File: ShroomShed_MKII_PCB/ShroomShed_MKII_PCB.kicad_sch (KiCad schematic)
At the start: 68 parts, among them J1 SWD 14 pin header, J2 TYPE-C-31-M-12, J3 Fan, J4 AUX_SPI, J5 SD_SPI, J6 DHT_I2C, J7 Display_Touch_SPI, J8 Front_Panel, J9 Transducer Driver, Q1 T2N7002AK, Q2 BC817, SW1 EVQ-Q2B03W, SW2 SW_SPDT, U1 AMS1117-3.3, U2 TPS61085DGK, U3 USBLC6-2SC6, U4 ENS210, U5 STM32H562VGTx, Y1 16MHz

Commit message: added solidworks files
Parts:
- removed J8: Front_Panel, DOWNLOAD_Connectors:CONN_532610001-SD_06_MOL, symbol Connector_Generic:Conn_01x06
- removed SW2: SW_SPDT, Button_Switch_SMD:SW_SPDT_PCM12, symbol Switch:SW_SPDT
- added J9: Control_Panel, DOWNLOAD_Connectors:CONN_532610001-SD_07_MOL, symbol Connector_Generic:Conn_01x07
- added SW3: FAN P SELECT, footprints:MST-22D18G2 3J, symbol Switch:SW_Push_SPDT
- C11: value 1000uf -> 1000uF
- C12, C14, C15: value 10uf -> 10uF
- C13: value 1uf -> 1uF
- C18, C20: value 100nf -> 100nF
- C19: value 1.1nf -> 1.1nF
- J4: JLCPCB Part # (none) -> C17393620
- J5, J6: JLCPCB Part # (none) -> C696092
- J7: JLCPCB Part # (none) -> C505101
- J8: renamed from J9; JLCPCB Part # (none) -> C293630
- R12: value 1K -> 1k
- renumbered D6 to D3, D3 to D4, R21 to R13, R13 to R14, R14 to R15, R15 to R16
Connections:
- net +3V3: now also SW3.1 (A)
- net ENCODER_BUTTON: now also J9.5 (Pin_5)
- net ENCODER_CHANNEL_A: now also J9.6 (Pin_6)
- net ENCODER_CHANNEL_B: now also J9.7 (Pin_7)
- net GND: now also J9.1 (Pin_1), SW3.3 (C)
- net LED_WATER: now also U5.83 (PD2), J9.2 (Pin_2); no longer U5.84 (PD3)
- net PUSH_BUTTON renamed BUTTON_1
- net BUTTON_1: now also J9.4 (Pin_4)
- new net BUTTON_2: J9.3 (Pin_3), U5.84 (PD3)

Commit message: source code template setup and blinky achieved
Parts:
- removed D3: Blue, LED_SMD:LED_0603_1608Metric, symbol Device:LED
- removed J4: AUX_SPI, DOWNLOAD_Connectors:CONN_532610001-SD_06_MOL, symbol Connector_Generic:Conn_01x06
- removed R13: 330r, Resistor_SMD:R_0603_1608Metric, symbol Device:R_Small
- removed R17: 2k2, Resistor_SMD:R_0603_1608Metric, symbol Device:R_Small
- added D5: TC5050RGBF08-3CJH-AF53A, symbol Custom_Symbols:LED_RGB_TC5050RGBF08
- added J4: SD_SPI, DOWNLOAD_Connectors:CONN_532610001-SD_04_MOL, symbol Connector_Generic:Conn_01x04
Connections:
- net +3V3: now also J4.1 (Pin_1)
- net GND: now also J4.4 (Pin_4); no longer Q2.2 (E)
- net SPI2_MISO: no longer names the net of U5.53 (PB14)
- net SPI2_MOSI: no longer names the net of U5.54 (PB15)
- net SPI2_NSS renamed UART5_RX
- net UART5_RX: now also J4.3 (Pin_3)
- net SPI2_SCK renamed UART5_TX
- net UART5_TX: now also J4.2 (Pin_2)
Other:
- note removed: "Humidifier LED"
- moved on the sheet: Q2

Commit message: finished V2.1 PCB
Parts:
- removed D4: Yellow, LED_SMD:LED_0603_1608Metric, symbol Device:LED
- removed J3: Fan, Connector_JST:JST_XH_B2B-XH-A_1x02_P2.50mm_Vertical, symbol Connector:Screw_Terminal_01x02
- removed J8: Transducer Driver, DOWNLOAD_Connectors:CONN_532610001-SD_03_MOL, symbol Connector_Generic:Conn_01x03
- removed J9: Control_Panel, DOWNLOAD_Connectors:CONN_532610001-SD_07_MOL, symbol Connector_Generic:Conn_01x07
- removed Q1: T2N7002AK, Package_TO_SOT_SMD:SOT-23, symbol Transistor_FET:T2N7002AK
- removed Q2: BC817, Package_TO_SOT_SMD:SOT-23, symbol Transistor_BJT:BC817
- removed R16: 10k, Resistor_SMD:R_0603_1608Metric, symbol Device:R
- removed R7: 2k2, Resistor_SMD:R_0603_1608Metric, symbol Device:R_Small
- added C2, C3, C7, C8: 1uF, Capacitor_SMD:C_0603_1608Metric, symbol Device:C
- added D10, D11, D12, D13, D2, D3, D4, D5, D6, D8, D9: XL-5050RGBC, LED_SMD:LED_RGB_5050-6, symbol Custom:XL-5050RGBC
- added D14: BLUE, LED_THT:LED_D4.0mm, symbol Device:LED
- added H1, H4: MountingHole_Pad, MountingHole:MountingHole_3.2mm_M3_Pad, symbol Mechanical:MountingHole_Pad
- added J3: Inputs, Connector_JST:JST_XH_B6B-XH-A_1x06_P2.50mm_Vertical, symbol Connector_Generic:Conn_01x06
- added J6: ERM, Connector_JST:JST_XH_S4B-XH-A-1_1x04_P2.50mm_Horizontal, symbol Connector_Generic:Conn_01x04
- added Q1: BC817, Package_TO_SOT_SMD:SOT-23, symbol Transistor_BJT:BC817
- added R1: 33r, Resistor_SMD:R_0603_1608Metric, symbol Device:R_Small
- added R11, R3, R4: 4k7, Resistor_SMD:R_0603_1608Metric, symbol Device:R_Small
- added R13: 5k1, Resistor_SMD:R_0603_1608Metric, symbol Device:R_Small
- added R16: 500r, Resistor_SMD:R_0603_1608Metric, symbol Device:R_Small
- added R17, R20: 10k, Resistor_SMD:R_0603_1608Metric, symbol Device:R_Small
- added U1, U2, U5, U6: WS2811, Package_SO:SOIC-8_3.9x4.9mm_P1.27mm, symbol Driver_LED:WS2811
- C15: renamed from C11; value 1000uF -> 470uF; footprint Capacitor_SMD:CP_Elec_10x10.5 -> Capacitor_SMD:CP_Elec_6.3x7.7; P# C5355001 -> C2977552
- D1: renamed from D5; value TC5050RGBF08-3CJH-AF53A -> XL-5050RGBC; footprint (none) -> LED_SMD:LED_RGB_5050-6; symbol Custom_Symbols:LED_RGB_TC5050RGBF08 -> Custom:XL-5050RGBC
- J2: renamed from J4; value SD_SPI -> UART; footprint DOWNLOAD_Connectors:CONN_532610001-SD_04_MOL -> Connector_PinHeader_2.00mm:PinHeader_1x04_P2.00mm_Vertical
- J4: renamed from J6; value DHT_I2C -> SHT31; footprint DOWNLOAD_Connectors:CONN_532610001-SD_04_MOL -> Connector_JST:JST_XH_S4B-XH-A-1_1x04_P2.50mm_Horizontal
- J7: renamed from J5; footprint DOWNLOAD_Connectors:CONN_532610001-SD_04_MOL -> Connector_PinSocket_2.54mm:PinSocket_1x04_P2.54mm_Vertical
- J8: renamed from J7; footprint DOWNLOAD_Connectors:CONN_532610001-SD_14_MOL -> Connector_PinSocket_2.54mm:PinSocket_1x14_P2.54mm_Vertical
- R10: value 2k2 -> 4k7
- R12: value 1k -> 5k1; DESCRIPTION C21190 -> (none); PACKAGE 0603 -> (none)
- R15: value 100R -> 1k; DESCRIPTION C22775 -> (none); PACKAGE 0603 -> (none)
- R18: renamed from R9; value 47r -> 33r
- SW2: renamed from SW3; value FAN P SELECT -> BOOT SELECT; footprint footprints:MST-22D18G2 3J -> Button_Switch_SMD:SW_SPDT_Shouhan_MSK12C02; P# (none) -> C431540
- renumbered C12 to C1, C15 to C10, C10 to C11, C20 to C12, C21 to C13, C22 to C14, C8 to C16, C9 to C17, C23 to C18, C24 to C19, C7 to C20, C1 to C21, C16 to C22, C2 to C23, C3 to C24, C17 to C25, C4 to C26, C5 to C27, C6 to C28, C13 to C4, C18 to C5, C19 to C6, C14 to C9, D1 to D15, D2 to D7, H1 to H3, J2 to J1, J1 to J5, R3 to R14, R14 to R19, R8 to R2, R4 to R21, R11 to R6, R1 to R7, R6 to R8, R2 to R9, U2 to U3, U3 to U4, U4 to U7, U1 to U8, U5 to U9
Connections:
- net +12V: now also D1.4 (BA), D1.5 (GA), D1.6 (RA), R10.1, D11.4 (BA), D11.5 (GA), D11.6 (RA), D14.2 (A), D4.4 (BA), D4.5 (GA), D4.6 (RA), D8.4 (BA), D8.5 (GA), D8.6 (RA), J6.1 (Pin_1), R11.1, R3.1, R4.1; no longer R12.1
- net +3V3: now also J8.14 (Pin_14), R12.2, R13.2, R17.1, R20.1; no longer J8.1 (Pin_1), R10.2
- net DISPLAY_DC: now also J8.10 (Pin_10); no longer J8.3 (Pin_3)
- net DISPLAY_LED: now also J8.7 (Pin_7), U9.95 (PB8); no longer J8.8 (Pin_8), U9.26 (PA3)
- net DISPLAY_MISO: now also J8.6 (Pin_6); no longer J8.5 (Pin_5)
- net DISPLAY_MOSI: now also J8.9 (Pin_9); no longer J8.6 (Pin_6)
- net DISPLAY_NSS: now also J8.12 (Pin_12); no longer J8.4 (Pin_4)
- net DISPLAY_RST: now also J8.11 (Pin_11); no longer J8.7 (Pin_7)
- net DISPLAY_SCK: now also J8.8 (Pin_8); no longer J8.2 (Pin_2)
- net ENCODER_CHANNEL_A: now also U9.60 (PD13), J3.1 (Pin_1); no longer U9.64 (PC7)
- net ENCODER_CHANNEL_B: now also U9.59 (PD12), J3.2 (Pin_2); no longer U9.63 (PC6)
- net ENS210_SCL: now also U9.47 (PB10), R13.1; no longer U9.92 (PB6)
- net ENS210_SDA: now also R12.1, U9.51 (PB12); no longer R10.1, U9.93 (PB7)
- net FAN_PWM: now also U9.36 (PB1), J6.3 (Pin_3); no longer R15.2, U9.24 (PA1)
- net GND: now also J8.13 (Pin_13), C2.2, C3.2, C7.2, C8.2, H1.1, H4.1, J3.6 (Pin_6), J6.4 (Pin_4), Q1.2 (E), U1.4 (GND), U2.4 (GND), U5.4 (GND), U6.4 (GND); no longer J8.14 (Pin_14)
- net SD_MISO: now also J7.2 (Pin_2), U9.31 (PA6); no longer J7.3 (Pin_3), U9.79 (PC11)
- net SD_MOSI: now also J7.3 (Pin_3), U9.32 (PA7); no longer J7.4 (Pin_4), U9.80 (PC12)
- net SD_NSS: now also J7.4 (Pin_4), U9.29 (PA4); no longer J7.1 (Pin_1), U9.77 (PA15(JTDI))
- net SD_SCK: now also J7.1 (Pin_1), U9.30 (PA5); no longer J7.2 (Pin_2), U9.78 (PC10)
- net SHT31_SCL: now also R20.2
- net SHT31_SDA: now also R17.2
- net SWD_SWO: no longer U9.89 (PB3(JTDO)
- net TOUCH_IRQ: now also J8.1 (Pin_1), U9.92 (PB6); no longer J8.13 (Pin_13), U9.33 (PC4)
- net TOUCH_MISO: now also J8.2 (Pin_2), U9.90 (PB4(NJTRST)); no longer J8.11 (Pin_11), U9.31 (PA6)
- net TOUCH_MOSI: now also J8.3 (Pin_3), U9.91 (PB5); no longer J8.12 (Pin_12), U9.32 (PA7)
- net TOUCH_NSS: now also J8.4 (Pin_4), U9.77 (PA15(JTDI)); no longer J8.9 (Pin_9), U9.29 (PA4)
- net TOUCH_SCK: now also J8.5 (Pin_5), U9.89 (PB3(JTDO); no longer J8.10 (Pin_10), U9.30 (PA5)
- net TRANSDUCER_PWM: now also U9.35 (PB0), J6.2 (Pin_2); no longer U9.44 (PE13)
- net UART4_RX: now also U9.81 (PD0); no longer U9.58 (PD11)
- net UART4_TX: now also U9.82 (PD1); no longer U9.59 (PD12)
- net WATER_LED: now reaches U9.16 (PC1)
- net WATER_LED: now also R15.2
- net RGB_MOSI: now reaches U9.18 (PC3)
- net RGB_MOSI: now also R1.1
- net RF_RX: now reaches U9.38 (PE7)
- net RF_RX: now also J2.3 (Pin_3)
- net RF_TX: now reaches U9.39 (PE8)
- net RF_TX: now also J2.2 (Pin_2)
- net INPUT_3: now reaches U9.56 (PD9)
- net INPUT_3: now also J3.5 (Pin_5)
- net INPUT_2: now reaches U9.57 (PD10)
- net INPUT_2: now also J3.4 (Pin_4)
- net at R15.1: now also Q1.1 (B)
- net at SW2.2 (B): now also R19.2
- net at D1.1 (RK): now also D2.6 (RA)
- net at D1.2 (GK): now also D2.5 (GA)
- net at D1.3 (BK): now also D2.4 (BA)
- net BUTTON_1: no longer names the net of U9.85 (PD4)
- net BUTTON_2: no longer names the net of U9.84 (PD3)
- net ENCODER_BUTTON: no longer names the net of U9.86 (PD5)
- net FAN_DETECT: no longer names the net of U9.25 (PA2)
- net LED_HUMIDIFIER: no longer names the net of U9.45 (PE14)
- net LED_WATER: no longer names the net of U9.83 (PD2)
- removed net UART5_RX: J2.3 (Pin_3), U9.51 (PB12)
- net UART5_TX: no longer names the net of U9.52 (PB13)
- net UART5_TX: no longer J2.2 (Pin_2)
- new net: D3.2 (GK), U1.1 (OUTR)
- new net: D3.3 (BK), U1.2 (OUTG)
- new net: D3.1 (RK), U1.3 (OUTB)
- new net: C2.1, R3.2, U1.8 (VDD)
- new net: C3.1, R4.2, U2.8 (VDD)
- new net: D10.6 (RA), D9.1 (RK)
- new net: D10.5 (GA), D9.2 (GK)
- new net: D10.4 (BA), D9.3 (BK)
- new net: D8.3 (BK), D9.4 (BA)
- new net: D8.2 (GK), D9.5 (GA)
- new net: D8.1 (RK), D9.6 (RA)
- new net: D6.2 (GK), U2.1 (OUTR)
- new net: D6.3 (BK), U2.2 (OUTG)
- new net: D6.1 (RK), U2.3 (OUTB)
- new net: D5.3 (BK), D6.4 (BA)
- new net: D5.2 (GK), D6.5 (GA)
- new net: D5.1 (RK), D6.6 (RA)
- new net: D10.2 (GK), U5.1 (OUTR)
- new net: D10.3 (BK), U5.2 (OUTG)
- new net: D10.1 (RK), U5.3 (OUTB)
- new net: C7.1, R10.2, U5.8 (VDD)
- new net: C8.1, R11.2, U6.8 (VDD)
- new net: D14.1 (K), R16.1
- new net: Q1.3 (C), R16.2
- new net: D11.1 (RK), D12.6 (RA)
- new net: D11.2 (GK), D12.5 (GA)
- new net: D11.3 (BK), D12.4 (BA)
- new net: D12.1 (RK), D13.6 (RA)
- new net: D12.2 (GK), D13.5 (GA)
- new net: D12.3 (BK), D13.4 (BA)
- new net: D13.2 (GK), U6.1 (OUTR)
- new net: D13.3 (BK), U6.2 (OUTG)
- new net: D13.1 (RK), U6.3 (OUTB)
- new net: D4.3 (BK), D5.4 (BA)
- new net: D4.2 (GK), D5.5 (GA)
- new net: D4.1 (RK), D5.6 (RA)
- new net: D2.1 (RK), D3.6 (RA)
- new net: D2.2 (GK), D3.5 (GA)
- new net: D2.3 (BK), D3.4 (BA)
- new net INPUT_1: J3.3 (Pin_3), U9.58 (PD11)
- new net RGBD_12_DIO: U1.5 (DO), U5.6 (DIN)
- new net RGBD_1_DIN: R1.2, U1.6 (DIN)
- new net RGBD_23_DIO: U5.5 (DO), U6.6 (DIN)
- new net RGBD_34_DIO: U2.6 (DIN), U6.5 (DO)
- no-connect marks 42 -> 27
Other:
- note added: "RGB LEDs"
- note added: "SHT31 I2C PU's"
- note added: "Water LED"
- note removed: "Fan Drive"
- moved on the sheet: C18, C19, D1, H2, H3, J2, J4, J7, J8, R19, SW2, U9

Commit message: got the display working thank fuck
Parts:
- C15: value 470uF -> 100uF; footprint Capacitor_SMD:CP_Elec_6.3x7.7 -> Capacitor_SMD:CP_Elec_6.3x5.4; P# C2977552 -> C2887276

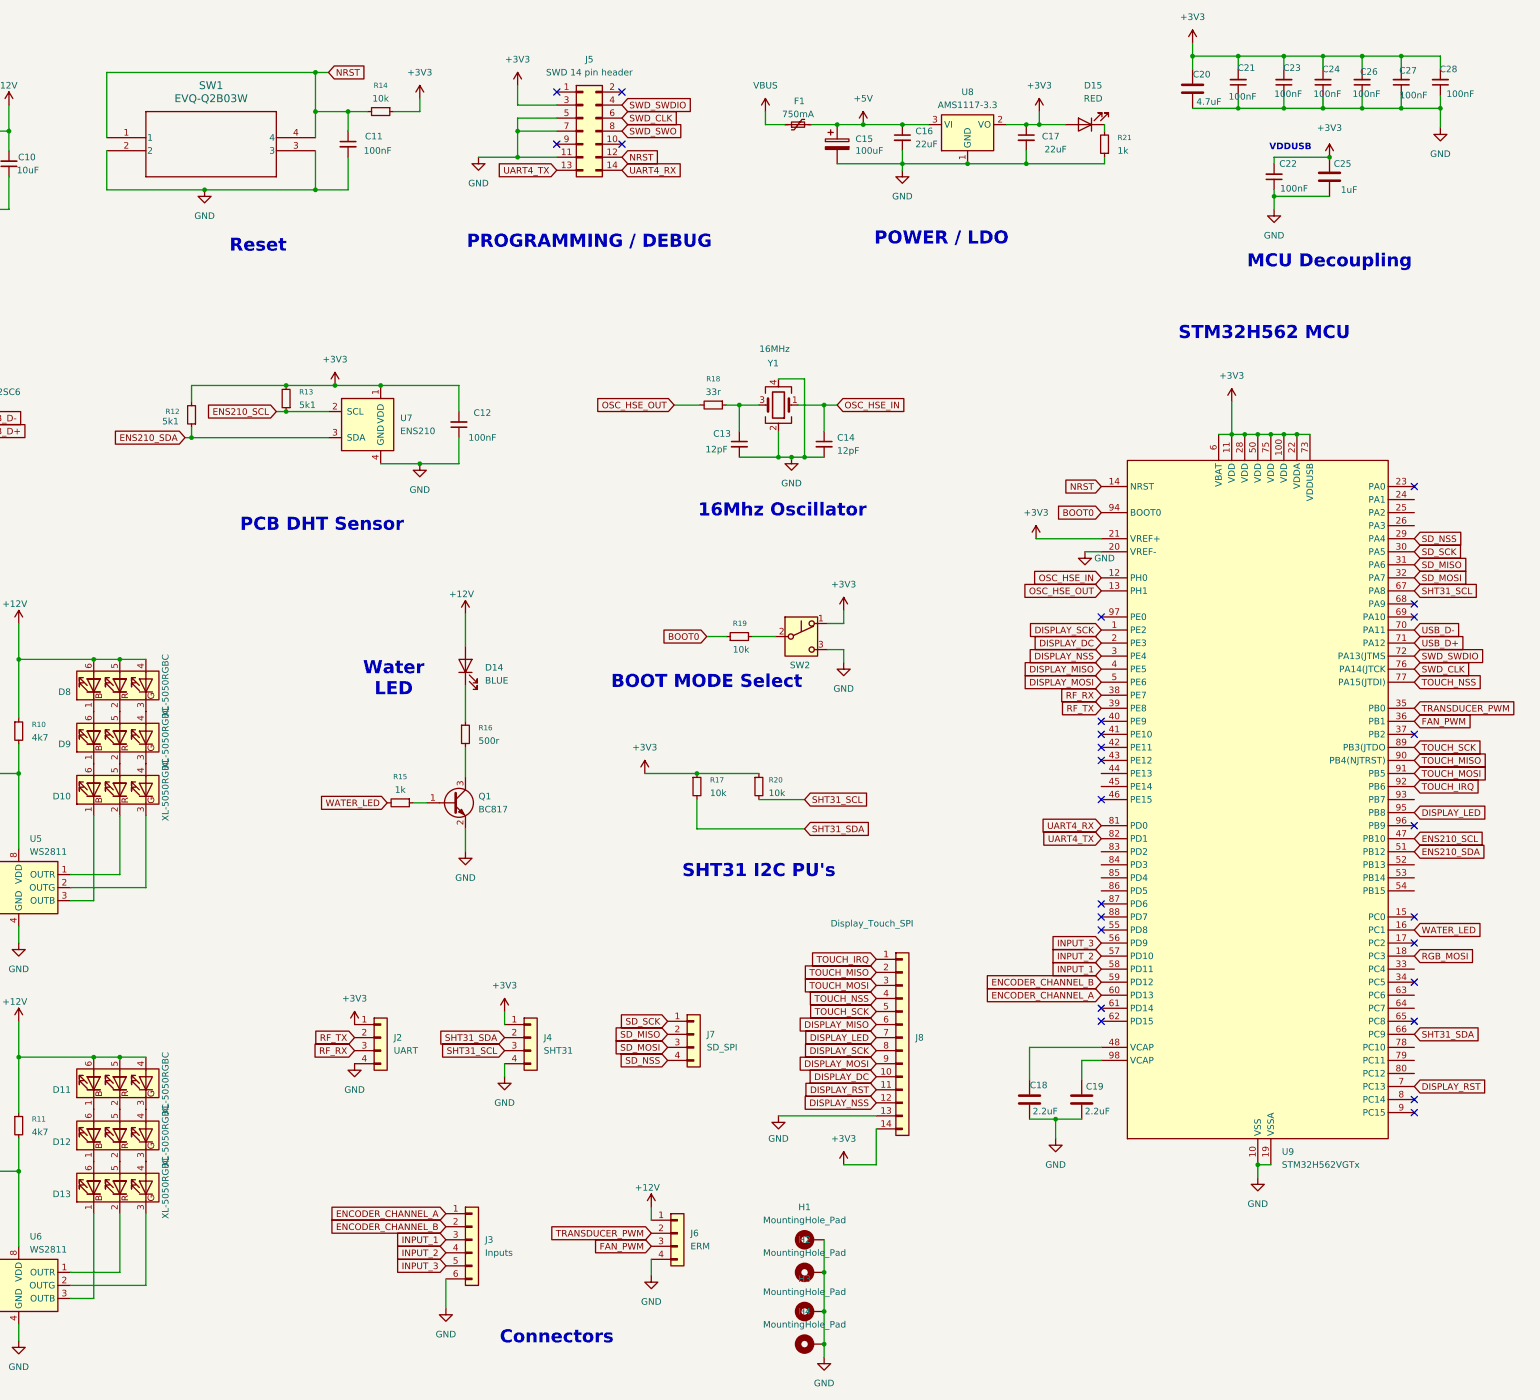
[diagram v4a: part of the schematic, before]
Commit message: completed controler V2.2, got basic blocking implementation of display SPI DMA working
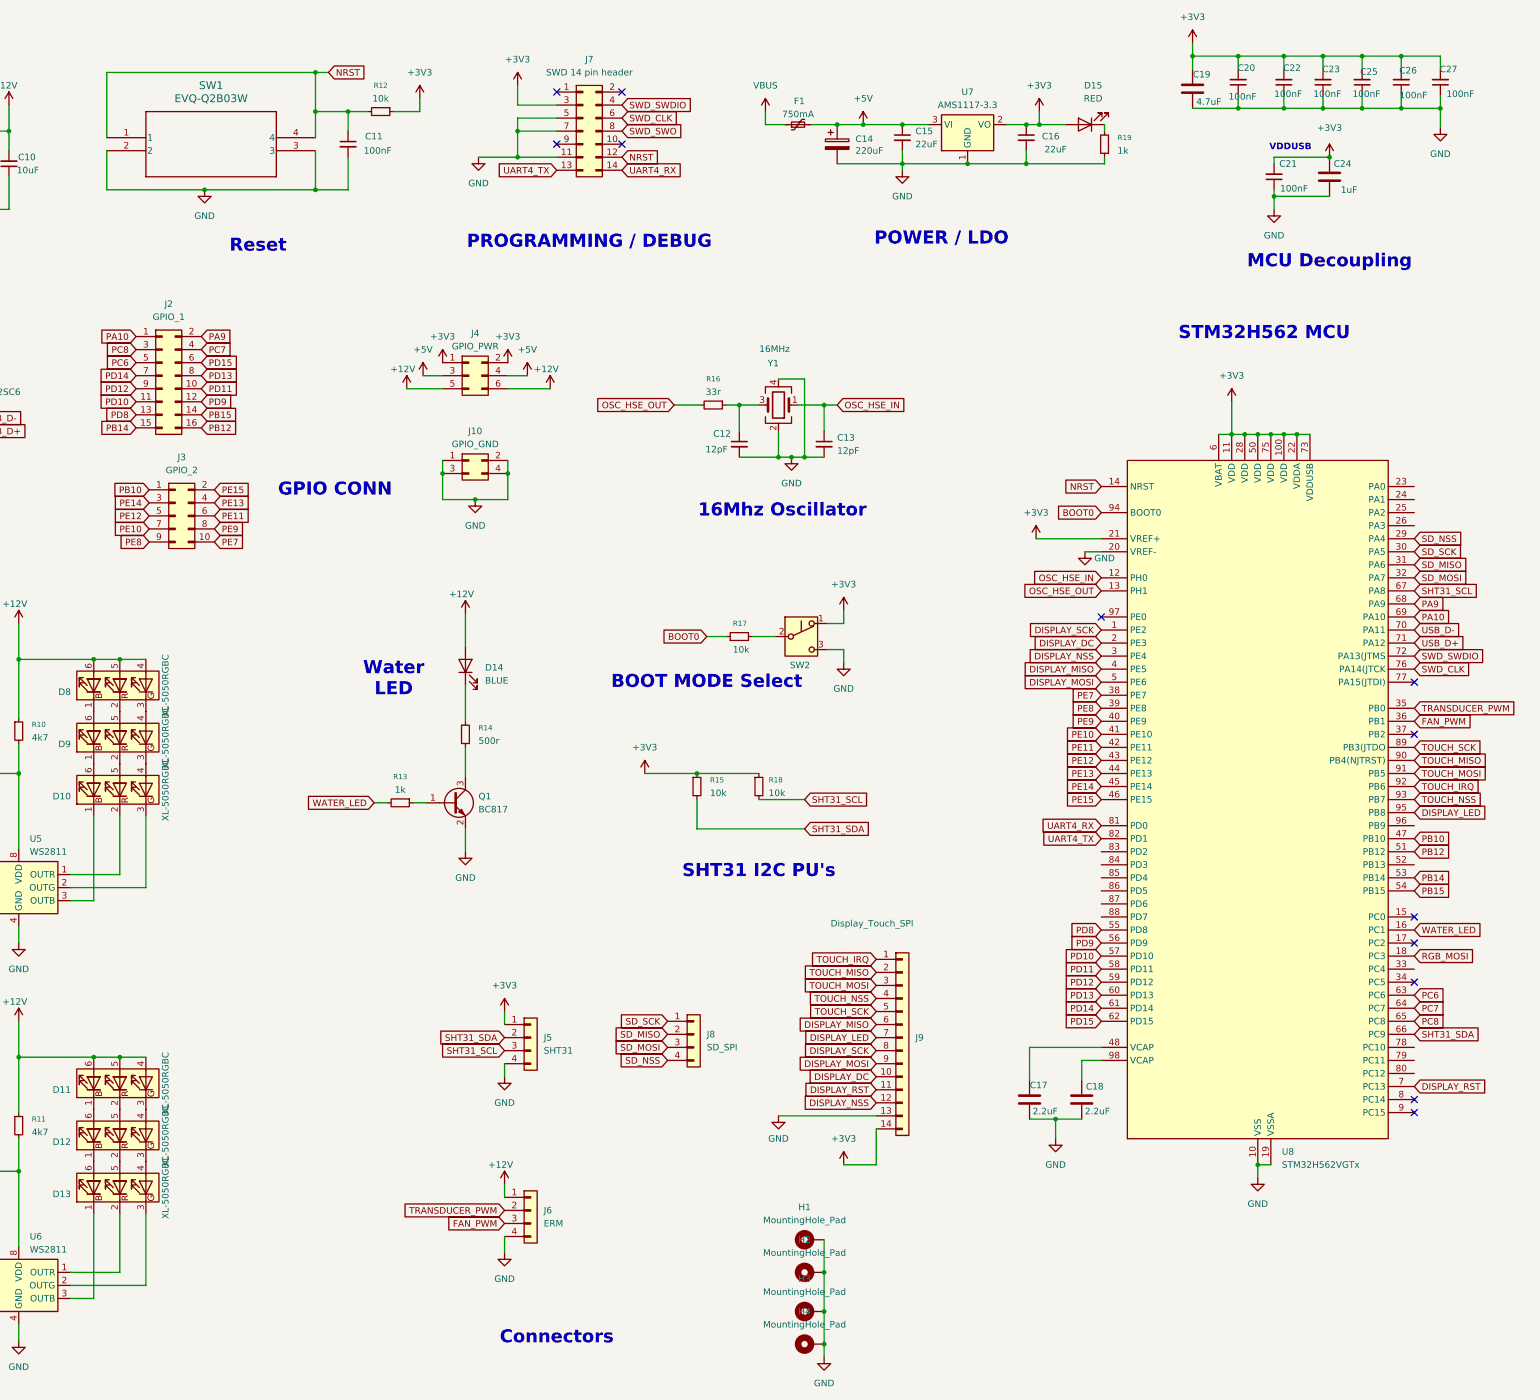
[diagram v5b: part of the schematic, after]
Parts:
- removed C12: 100nF, Capacitor_SMD:C_0603_1608Metric, symbol Device:C_Small
- removed J2: UART, Connector_PinHeader_2.00mm:PinHeader_1x04_P2.00mm_Vertical, symbol Connector_Generic:Conn_01x04
- removed J3: Inputs, Connector_JST:JST_XH_B6B-XH-A_1x06_P2.50mm_Vertical, symbol Connector_Generic:Conn_01x06
- removed R12, R13: 5k1, Resistor_SMD:R_0603_1608Metric, symbol Device:R_Small
- removed U7: ENS210, Package_DFN_QFN:AMS_QFN-4-1EP_2x2mm_P0.95mm_EP0.7x1.6mm, symbol Sensor_Humidity:ENS210
- added J10: GPIO_GND, Connector_PinHeader_2.54mm:PinHeader_2x02_P2.54mm_Vertical, symbol Connector_Generic:Conn_02x02_Odd_Even
- added J2: GPIO_1, Connector_PinHeader_2.54mm:PinHeader_2x08_P2.54mm_Vertical, symbol Connector_Generic:Conn_02x08_Odd_Even
- added J3: GPIO_2, Connector_PinHeader_2.54mm:PinHeader_2x05_P2.54mm_Vertical, symbol Connector_Generic:Conn_02x05_Odd_Even
- added J4: GPIO_PWR, Connector_PinHeader_2.54mm:PinHeader_2x03_P2.54mm_Vertical, symbol Connector_Generic:Conn_02x03_Odd_Even
- C14: renamed from C15; value 100uF -> 220uF
- H1, H2, H3, H4: footprint MountingHole:MountingHole_3.2mm_M3_Pad -> MountingHole:MountingHole_3.2mm_M3_Pad_Via
- renumbered C13 to C12, C14 to C13, C16 to C15, C17 to C16, C18 to C17, C19 to C18, C20 to C19, C21 to C20, C22 to C21, C23 to C22, C24 to C23, C25 to C24, C26 to C25, C27 to C26, C28 to C27, J4 to J5, J5 to J7, J7 to J8, J8 to J9, R14 to R12, R15 to R13, R16 to R14, R17 to R15, R18 to R16, R19 to R17, R20 to R18, R21 to R19, U8 to U7, U9 to U8
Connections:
- net +12V: now also J4.5 (Pin_5), J4.6 (Pin_6)
- net +3V3: now also J4.1 (Pin_1), J4.2 (Pin_2)
- net +5V: now also J4.3 (Pin_3), J4.4 (Pin_4)
- net GND: now also J10.1 (Pin_1), J10.2 (Pin_2), J10.3 (Pin_3), J10.4 (Pin_4)
- net TOUCH_NSS: now also U8.93 (PB7); no longer U8.77 (PA15(JTDI))
- net PE9: now reaches U8.40 (PE9)
- net PE9: now also J3.8 (Pin_8)
- net PE10: now reaches U8.41 (PE10)
- net PE10: now also J3.7 (Pin_7)
- net PE11: now reaches U8.42 (PE11)
- net PE11: now also J3.6 (Pin_6)
- net PE12: now reaches U8.43 (PE12)
- net PE12: now also J3.5 (Pin_5)
- net PE13: now reaches U8.44 (PE13)
- net PE13: now also J3.4 (Pin_4)
- net PE14: now reaches U8.45 (PE14)
- net PE14: now also J3.3 (Pin_3)
- net PE15: now reaches U8.46 (PE15)
- net PE15: now also J3.2 (Pin_2)
- net PB14: now reaches U8.53 (PB14)
- net PB14: now also J2.15 (Pin_15)
- net PB15: now reaches U8.54 (PB15)
- net PB15: now also J2.14 (Pin_14)
- net PD8: now reaches U8.55 (PD8)
- net PD8: now also J2.13 (Pin_13)
- net PD14: now reaches U8.61 (PD14)
- net PD14: now also J2.7 (Pin_7)
- net PD15: now reaches U8.62 (PD15)
- net PD15: now also J2.6 (Pin_6)
- net PC6: now reaches U8.63 (PC6)
- net PC6: now also J2.5 (Pin_5)
- net PC7: now reaches U8.64 (PC7)
- net PC7: now also J2.4 (Pin_4)
- net PC8: now reaches U8.65 (PC8)
- net PC8: now also J2.3 (Pin_3)
- net PA9: now reaches U8.68 (PA9)
- net PA9: now also J2.2 (Pin_2)
- net PA10: now reaches U8.69 (PA10)
- net PA10: now also J2.1 (Pin_1)
- net ENCODER_CHANNEL_A renamed PD13
- net PD13: now also J2.8 (Pin_8)
- net ENCODER_CHANNEL_B renamed PD12
- net PD12: now also J2.9 (Pin_9)
- net ENS210_SCL renamed PB10
- net PB10: now also J3.1 (Pin_1)
- net ENS210_SDA renamed PB12
- net PB12: now also J2.16 (Pin_16)
- net INPUT_1 renamed PD11
- net PD11: now also J2.10 (Pin_10)
- net INPUT_2 renamed PD10
- net PD10: now also J2.11 (Pin_11)
- net INPUT_3 renamed PD9
- net PD9: now also J2.12 (Pin_12)
- net RF_RX renamed PE7
- net PE7: now also J3.10 (Pin_10)
- net RF_TX renamed PE8
- net PE8: now also J3.9 (Pin_9)
- no-connect marks 27 -> 13
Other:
- note added: "GPIO CONN"
- note removed: "PCB DHT Sensor"
- moved on the sheet: J6

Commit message: Fixed distance between display pin headers, checkpoint for proper DMA implementation
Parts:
- removed J10: GPIO_GND, Connector_PinHeader_2.54mm:PinHeader_2x02_P2.54mm_Vertical, symbol Connector_Generic:Conn_02x02_Odd_Even
- removed J4: GPIO_PWR, Connector_PinHeader_2.54mm:PinHeader_2x03_P2.54mm_Vertical, symbol Connector_Generic:Conn_02x03_Odd_Even
- added J4: 3V3_PWR, Connector_PinHeader_2.54mm:PinHeader_2x02_P2.54mm_Vertical, symbol Connector_Generic:Conn_02x02_Odd_Even
- added J5: 5V_PWR, Connector_PinHeader_2.54mm:PinHeader_2x02_P2.54mm_Vertical, symbol Connector_Generic:Conn_02x02_Odd_Even
- added J6: 12V_PWR, Connector_PinHeader_2.54mm:PinHeader_2x02_P2.54mm_Vertical, symbol Connector_Generic:Conn_02x02_Odd_Even
- renumbered J8 to J10, J9 to J11, J5 to J7, J6 to J8, J7 to J9
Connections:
- net +12V: now also J6.1 (Pin_1), J6.2 (Pin_2)
- net +3V3: now also J4.1 (Pin_1), J4.2 (Pin_2)
- net +5V: now also J5.1 (Pin_1), J5.2 (Pin_2); no longer U3.3 (EN)
- net GND: now also J4.3 (Pin_3), J4.4 (Pin_4), J5.3 (Pin_3), J5.4 (Pin_4), J6.3 (Pin_3), J6.4 (Pin_4)
- net BOOST_EN: now reaches U8.25 (PA2)
- net BOOST_EN: now also U3.3 (EN)
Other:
- moved on the sheet: J2

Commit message: Controller V2.2 ordered
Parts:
- C1, C10, C9: DESCRIPTION C19702 -> (none)
- C4: DESCRIPTION C15849 -> (none)
- C5: DESCRIPTION C14663 -> (none)
- C6: DESCRIPTION C710889 -> (none)
- D7: DESCRIPTION C2479 -> (none)
- L1: DESCRIPTION C182156 -> (none)
- R5: DESCRIPTION C23196 -> (none)
- R7: DESCRIPTION C25803 -> (none)
- R8: DESCRIPTION C23254 -> (none)
- R9: DESCRIPTION C23206 -> (none)
- U3: DESCRIPTION C113659 -> (none)
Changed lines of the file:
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@@
 (kicad_sch
-	(version 20250114)
+	(version 20260306)
 	(generator "eeschema")
-	(generator_version "9.0")
+	(generator_version "10.0")
 	(paper "A3")
 	(title_block
